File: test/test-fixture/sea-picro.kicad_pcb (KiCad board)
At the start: 2 copper layers, 0 parts

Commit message: tester footprints setup
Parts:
- added C1: 10u, Capacitor_SMD:C_0603_1608Metric, F.Cu at (192.3, 72.7)
- added C10: 100n, Capacitor_SMD:C_0603_1608Metric, F.Cu at (173.1, 56.8)
- added C11: 100n, Capacitor_SMD:C_0603_1608Metric, F.Cu at (190.0, 68.6)
- added C2: 4u7, Capacitor_SMD:C_0603_1608Metric, F.Cu at (170.3, 67.1)
- added C3: 100n, Capacitor_SMD:C_0603_1608Metric, F.Cu at (196.2, 77.9)
- added C4: 100n, Capacitor_SMD:C_0603_1608Metric, F.Cu at (182.5, 60.3)
- added C5: 100n, Capacitor_SMD:C_0603_1608Metric, F.Cu at (198.7, 76.8)
- added C6: 4u7, Capacitor_SMD:C_0603_1608Metric, F.Cu at (207.4, 88.1)
- added C7: 100n, Capacitor_SMD:C_0603_1608Metric, F.Cu at (180.6, 56.1)
- added C8: 100n, Capacitor_SMD:C_0603_1608Metric, F.Cu at (203.1, 84.1)
- added C9: 100n, Capacitor_SMD:C_0603_1608Metric, F.Cu at (168.4, 40.7)
- added D1: WS2812B, LED_SMD:LED_WS2812B_PLCC4_5.0x5.0mm_P3.2mm, F.Cu at (88.3, 121.9)
- added D2: RED, LED_THT:LED_D5.0mm, F.Cu at (127.1, 137.5)
- added D3: GRN, LED_THT:LED_D5.0mm, F.Cu at (125.4, 123.3)
- added F1: 500mA, josh-passives-smt:Fuse_0603_1608Metric, F.Cu at (180.0, 60.1)
- added F2: 500mA, josh-passives-smt:Fuse_0603_1608Metric, F.Cu at (209.9, 88.3)
- added H1: M3, MountingHole:MountingHole_3.2mm_M3_Pad_Via, F.Cu at (146.5, 80.0)
- added H2: M3, MountingHole:MountingHole_3.2mm_M3_Pad_Via, F.Cu at (146.5, 31.0)
- added H3: M3, MountingHole:MountingHole_3.2mm_M3_Pad_Via, F.Cu at (88.5, 80.0)
- added H4: M3, MountingHole:MountingHole_3.2mm_M3_Pad_Via, F.Cu at (88.5, 31.0)
- added H5: M3, MountingHole:MountingHole_3.2mm_M3_Pad_Via, F.Cu at (150.0, 147.3)
- added H6: M3, MountingHole:MountingHole_3.2mm_M3_Pad_Via, F.Cu at (86.7, 142.4)
- added J1: USB_C_Receptacle_USB2.0, josh-connectors:USB_C_Receptacle_HRO_TYPE-C-31-M-12, F.Cu at (167.9, 97.3)
- added J10: RST, Connector_PinHeader_2.54mm:PinHeader_1x03_P2.54mm_Vertical, F.Cu at (182.8, 79.9)
- added J11: SWDCLK, Connector_PinHeader_2.54mm:PinHeader_1x03_P2.54mm_Vertical, F.Cu at (171.3, 71.4)
- added J12: SWD, josh-connectors:SAMTEC_FTSH-105-01-L-DV-R-TR, F.Cu at (195.8, 98.5)
- added J13: SWDIO, Connector_PinHeader_2.54mm:PinHeader_1x03_P2.54mm_Vertical, F.Cu at (195.8, 93.8)
- added J2: Sea-Picro, josh-module:Sea-Picro_EXT_Pogo_Pins, F.Cu at (117.7, 92.8)
- added J3: SP_PWR, Connector_PinHeader_2.54mm:PinHeader_1x02_P2.54mm_Vertical, F.Cu at (164.4, 53.1)
- added J4: Raspberry_Pi_2_3, Connector_PinSocket_2.54mm:PinSocket_2x20_P2.54mm_Vertical, B.Cu at (93.4, 32.3)
- added J5: D- SEL, Connector_PinHeader_2.54mm:PinHeader_1x03_P2.54mm_Vertical, F.Cu at (164.4, 62.4)
- added J6: D+ SEL, Connector_PinHeader_2.54mm:PinHeader_1x03_P2.54mm_Vertical, F.Cu at (164.4, 57.7)
- added J7: USB_PWR, Connector_PinHeader_2.54mm:PinHeader_1x02_P2.54mm_Vertical, F.Cu at (198.8, 89.2)
- added J8: USB_C_Receptacle_USB2.0, josh-connectors:USB_C_Receptacle_HRO_TYPE-C-31-M-12, F.Cu at (201.9, 116.5)
- added J9: SSD1306 OLED, josh-module:OLED_SSD1306_I2C_0.96, F.Cu at (108.4, 116.0)
- added N1: Toggle Clamp, josh-mechanical:GH-201A_X_Adj, F.Cu at (117.6, 62.6)
- added R1: 5K1, Resistor_SMD:R_0603_1608Metric, F.Cu at (196.2, 73.9)
- added R10: 0R0, Resistor_SMD:R_0603_1608Metric, F.Cu at (163.4, 40.6)
- added R11: 0R0, Resistor_SMD:R_0603_1608Metric, F.Cu at (208.1, 80.1)
- added R12: 0R0, Resistor_SMD:R_0603_1608Metric, F.Cu at (178.1, 56.1)
- added R13: 0R0, Resistor_SMD:R_0603_1608Metric, F.Cu at (163.4, 36.6)
- added R14: 0R0, Resistor_SMD:R_0603_1608Metric, F.Cu at (168.4, 44.7)
- added R15: 0R0, Resistor_SMD:R_0603_1608Metric, F.Cu at (203.1, 80.1)
- added R16: 0R0, Resistor_SMD:R_0603_1608Metric, F.Cu at (192.5, 64.7)
- added R17: 0R0, Resistor_SMD:R_0603_1608Metric, F.Cu at (185.0, 60.3)
- added R18: 0R0, Resistor_SMD:R_0603_1608Metric, F.Cu at (182.3, 64.3)
- added R19: 0R0, Resistor_SMD:R_0603_1608Metric, F.Cu at (200.6, 84.9)
- added R2: 10K, Resistor_SMD:R_0603_1608Metric, F.Cu at (208.1, 84.1)
- added R20: 0R0, Resistor_SMD:R_0603_1608Metric, F.Cu at (210.7, 84.3)
- added R21: 0R0, Resistor_SMD:R_0603_1608Metric, F.Cu at (177.5, 60.1)
- added R22: 0R0, Resistor_SMD:R_0603_1608Metric, F.Cu at (180.6, 52.1)
- added R23: 0R0, Resistor_SMD:R_0603_1608Metric, F.Cu at (195.0, 69.8)
- added R24: 0R0, Resistor_SMD:R_0603_1608Metric, F.Cu at (200.6, 80.9)
- added R25: 0R0, Resistor_SMD:R_0603_1608Metric, F.Cu at (170.9, 44.8)
- added R26: 0R0, Resistor_SMD:R_0603_1608Metric, F.Cu at (192.5, 68.7)
- added R27: 0R0, Resistor_SMD:R_0603_1608Metric, F.Cu at (163.4, 44.6)
- added R28: 0R0, Resistor_SMD:R_0603_1608Metric, F.Cu at (183.1, 56.2)
- added R29: 0R0, Resistor_SMD:R_0603_1608Metric, F.Cu at (165.9, 40.6)
- added R3: 5K1, Resistor_SMD:R_0603_1608Metric, F.Cu at (187.5, 68.6)
- added R30: 0R0, Resistor_SMD:R_0603_1608Metric, F.Cu at (204.9, 88.1)
- added R31: 0R0, Resistor_SMD:R_0603_1608Metric, F.Cu at (203.7, 76.1)
- added R32: 0R0, Resistor_SMD:R_0603_1608Metric, F.Cu at (178.1, 52.1)
- added R33: 10K, Resistor_SMD:R_0603_1608Metric, F.Cu at (173.1, 52.8)
- added R34: 10K, Resistor_SMD:R_0603_1608Metric, F.Cu at (187.3, 64.3)
- added R35: 1K, Resistor_SMD:R_0603_1608Metric, F.Cu at (168.1, 48.7)
- added R36: 1K, Resistor_SMD:R_0603_1608Metric, F.Cu at (205.6, 80.1)
- added R37: 10K, Resistor_SMD:R_0603_1608Metric, F.Cu at (165.9, 44.6)
- added R38: 10K, Resistor_SMD:R_0603_1608Metric, F.Cu at (175.6, 56.1)
- added R39: 0R0, Resistor_SMD:R_0603_1608Metric, F.Cu at (175.9, 48.1)
- added R4: 0R0, Resistor_SMD:R_0603_1608Metric, F.Cu at (175.6, 52.1)
- added R40: 10K, Resistor_SMD:R_0603_1608Metric, F.Cu at (170.6, 48.8)
- added R41: 10K, Resistor_SMD:R_0603_1608Metric, F.Cu at (201.2, 76.1)
- added R42: 0R, Resistor_SMD:R_0603_1608Metric, F.Cu at (189.8, 64.6)
- added R43: 100K, Resistor_SMD:R_0603_1608Metric, F.Cu at (198.7, 72.8)
- added R44: 100K, Resistor_SMD:R_0603_1608Metric, F.Cu at (209.7, 92.3)
- added R5: 0R0, Resistor_SMD:R_0603_1608Metric, F.Cu at (173.4, 48.1)
- added R6: 4K7, Resistor_SMD:R_0603_1608Metric, F.Cu at (205.6, 84.1)
- added R7: 4K7, Resistor_SMD:R_0603_1608Metric, F.Cu at (184.8, 64.3)
- added R8: 100K, Resistor_SMD:R_0603_1608Metric, F.Cu at (187.6, 60.3)
- added R9: 0R0, Resistor_SMD:R_0603_1608Metric, F.Cu at (170.6, 53.4)
- added RN1: 1K, Resistor_SMD:R_Array_Convex_4x0603, F.Cu at (197.0, 81.9)
- added RN2: 1K, Resistor_SMD:R_Array_Convex_4x0603, F.Cu at (192.5, 76.8)
- added RN3: 1K, Resistor_SMD:R_Array_Convex_4x0603, F.Cu at (206.0, 92.2)
- added RN4: 1K, Resistor_SMD:R_Array_Convex_4x0603, F.Cu at (178.6, 64.2)
- added RN5: 1K, Resistor_SMD:R_Array_Convex_4x0603, F.Cu at (188.6, 72.6)
- added RN6: 1K, Resistor_SMD:R_Array_Convex_4x0603, F.Cu at (164.5, 48.7)
- added SW1: PASS, josh-buttons-switches:SW_Push_PTS645, F.Cu at (136.6, 123.5)
- added SW2: FAIL, josh-buttons-switches:SW_Push_PTS645, F.Cu at (137.3, 137.9)
- added SW3: SW_SPDT, josh-buttons-switches:SW_SPDT_PCM12, F.Cu at (165.1, 69.6)
- added SW4: SW_SPDT, josh-buttons-switches:SW_SPDT_PCM12, F.Cu at (199.1, 105.7)
- added SW5: SW_SPDT, josh-buttons-switches:SW_SPDT_PCM12, F.Cu at (176.5, 78.7)
- added SW6: SW_SPDT, josh-buttons-switches:SW_SPDT_PCM12, F.Cu at (185.0, 87.1)
- added TP1: SP_SWDIO, josh-test-point:TestPoint_Pogo_1.4mm_Drill_Off_Center, F.Cu at (126.9, 88.4)
- added TP2: SP_SWDCLK, josh-test-point:TestPoint_Pogo_1.4mm_Drill_Off_Center, F.Cu at (126.4, 97.1)
- added TP3: SP_RUN, josh-test-point:TestPoint_Pogo_1.4mm_Drill_Off_Center, F.Cu at (129.1, 91.2)
- added TP4: SP_BOOT, josh-test-point:TestPoint_Pogo_1.4mm_Drill_Off_Center, F.Cu at (128.7, 88.4)
- added U1: AP22653, Package_TO_SOT_SMD:SOT-23-6, F.Cu at (192.4, 81.4)
- added U2: USBLC6-2SC6, Package_TO_SOT_SMD:SOT-23-6, F.Cu at (208.8, 114.6)
- added U3: USBLC6-2SC6, Package_TO_SOT_SMD:SOT-23-6, F.Cu at (174.0, 61.4)
- added U4: 74HC595, Package_SO:SOIC-16_3.9x9.9mm_P1.27mm, F.Cu at (167.8, 78.8)
- added U5: 74HC595, Package_SO:SOIC-16_3.9x9.9mm_P1.27mm, F.Cu at (179.3, 98.9)
- added U6: 74HC595, Package_SO:SOIC-16_3.9x9.9mm_P1.27mm, F.Cu at (167.8, 87.2)
- added U7: ADC101C027CIMK, Package_TO_SOT_SMD:SOT-23-6, F.Cu at (208.8, 119.8)
- added U8: ADC101C027CIMK, Package_TO_SOT_SMD:SOT-23-6, F.Cu at (174.0, 66.5)

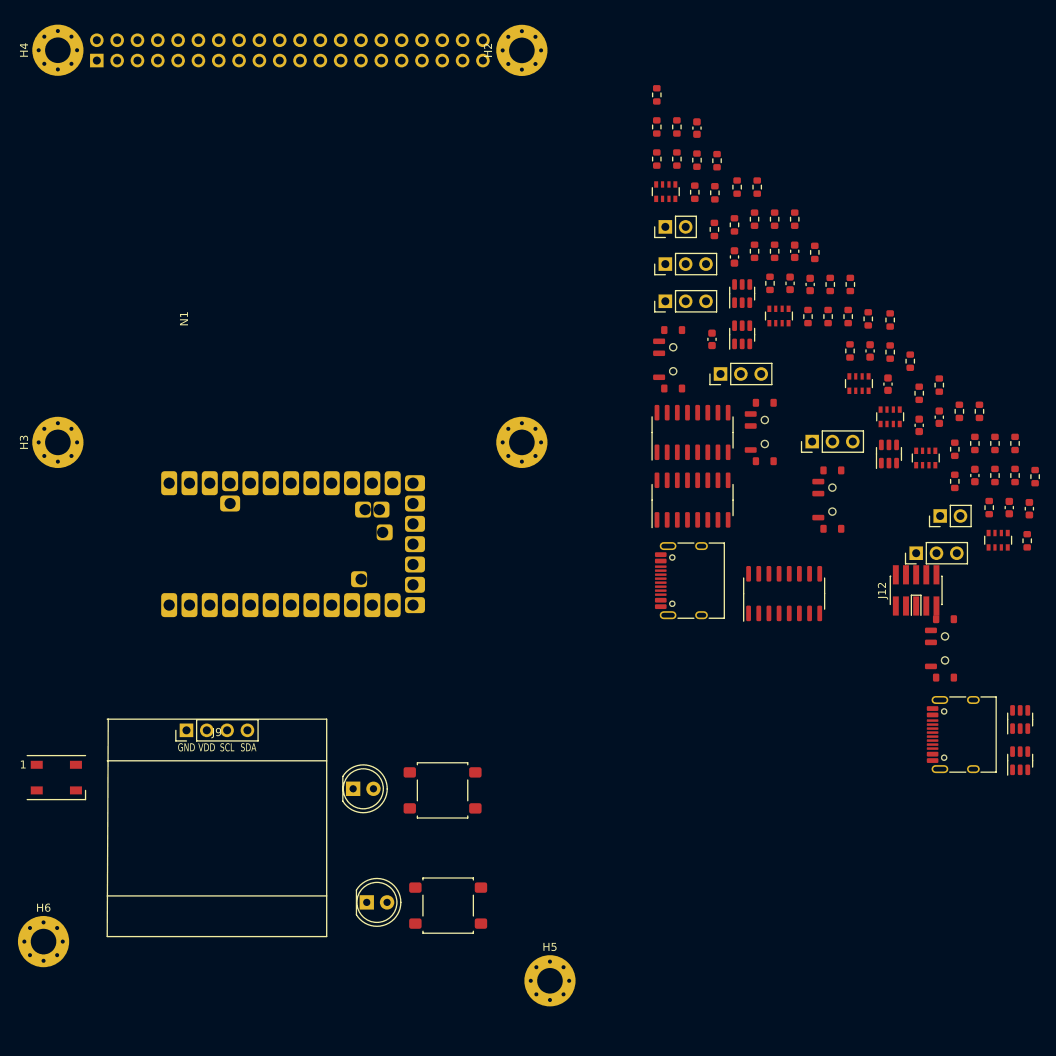
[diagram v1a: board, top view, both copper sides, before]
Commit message: rough mechanical layout
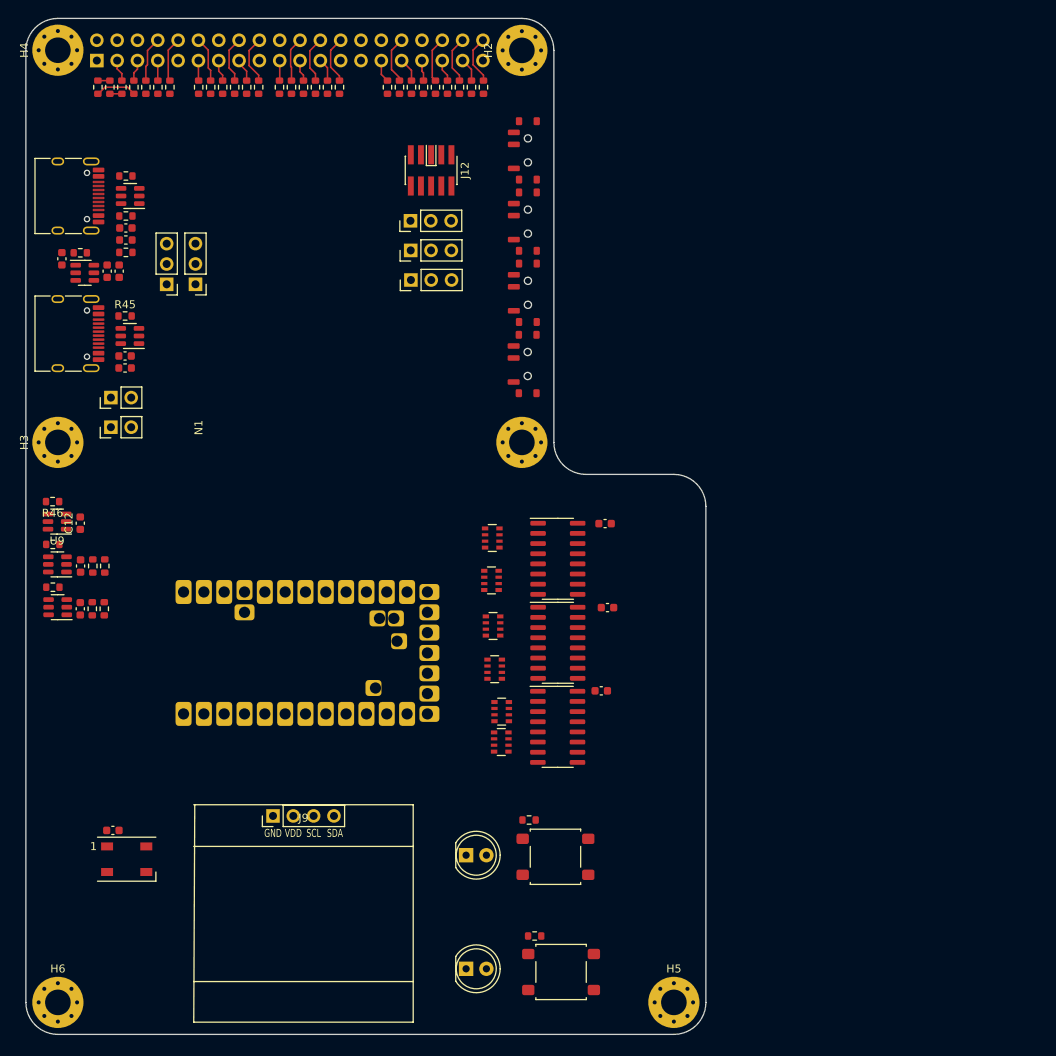
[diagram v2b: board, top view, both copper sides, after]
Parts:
- removed R35, R36: 1K, Resistor_SMD:R_0603_1608Metric
- removed R40, R41: 10K, Resistor_SMD:R_0603_1608Metric
- added C12: 100n, Capacitor_SMD:C_0603_1608Metric, F.Cu at (91.3, 90.1)
- added R45: 5K1, Resistor_SMD:R_0603_1608Metric, F.Cu at (96.9, 64.2)
- added R46: 0R0, Resistor_SMD:R_0603_1608Metric, F.Cu at (87.8, 87.4)
- added U9: ADC101C027CIMK, Package_TO_SOT_SMD:SOT-23-6, F.Cu at (88.4, 89.9)
- R18, R20, R22, R24, R26, R28: value 0R0 -> 10K
- R31, R32: value 0R0 -> 1K
- moved U2 129.1 mm to (97.5, 49.2), turned to 180 degrees
- moved J8 123.0 mm to (89.5, 66.4), turned to -90 degrees
- moved U7 121.8 mm to (88.5, 100.6), turned to 180 degrees
- moved R6 120.8 mm to (95.0, 35.6), turned to -90 degrees
- moved R44 116.8 mm to (92.9, 95.5), turned to -90 degrees
- moved R2 114.6 mm to (97.0, 56.2), turned to 0 degrees
- moved F2 114.4 mm to (96.9, 70.7), turned to 180 degrees
- moved C3 112.8 mm to (95.4, 128.5), turned to 0 degrees
- moved C6 112.1 mm to (96.9, 69.2), turned to 0 degrees
- moved C5 111.4 mm to (89.0, 57.0)
- moved R11 111.3 mm to (106.1, 35.6)
- moved R43 109.5 mm to (92.8, 100.8), turned to -90 degrees
- moved R30 109.3 mm to (109.1, 35.6)
- moved R42 105.8 mm to (87.9, 92.8), turned to 0 degrees
- moved J7 104.7 mm to (95.1, 74.4)
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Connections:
- D2 pad 1: Net-(D2-Pad1) -> /LED_FAIL
- D3 pad 1: Net-(D3-Pad1) -> /LED_PASS
- J8 pad A5: unconnected-(J8-PadA5) -> /CC_SENSE
- J8 pad B5: unconnected-(J8-PadB5) -> /CC_SENSE
- R37 pad 1: +3V3 -> /SP_VBUS
- R37 pad 2: /SHORT_DETECT_5V0 -> /SHT_CTRL_5V
- R38 pad 1: +3V3 -> +3.3VP
- R38 pad 2: /SHORT_DETECT_3V3 -> /SHT_CTRL_3V3
- R43 pad 1: /SHORT_DETECT_5V0 -> /SHT_CTRL_5V
- R44 pad 1: /SHORT_DETECT_3V3 -> /SHT_CTRL_3V3
- U3 pad 1: /USB_HOST- -> /USB_HOST+
- U3 pad 3: /USB_HOST+ -> /USB_HOST-
- U3 pad 4: Net-(J8-PadA6) -> Net-(J8-PadA7)
- U3 pad 6: Net-(J8-PadA7) -> Net-(J8-PadA6)
- U7 pad 3: /SHORT_DETECT_5V0 -> /SHT_CTRL_5V
- U8 pad 3: /SHORT_DETECT_3V3 -> /SHT_CTRL_3V3
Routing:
- net Net-(J4-Pad40): track 0.00 -> 6.09 mm
- net Net-(J4-Pad18): track 0.00 -> 6.08 mm
- net Net-(J4-Pad26): track 0.00 -> 6.02 mm
- net Net-(J4-Pad32): track 0.00 -> 5.99 mm
- net Net-(J4-Pad38): track 0.00 -> 5.95 mm
- net Net-(J4-Pad24): track 0.00 -> 5.88 mm
- net Net-(J4-Pad16): track 0.00 -> 5.85 mm
- net Net-(J4-Pad36): track 0.00 -> 5.73 mm
- net Net-(J4-Pad12): track 0.00 -> 5.68 mm
- net Net-(J4-Pad8): track 0.00 -> 5.66 mm
- net Net-(J4-Pad10): track 0.00 -> 5.64 mm
- net Net-(J4-Pad22): track 0.00 -> 5.57 mm
- net /I2C_SCL: track 0.00 -> 5.20 mm
- net Net-(J4-Pad31): track 0.00 -> 3.01 mm
- net Net-(J4-Pad37): track 0.00 -> 2.96 mm
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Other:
- board outline added: 85 x 127 mm

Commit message: test/quick-test-fixture
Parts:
- added H7: M2, MountingHole:MountingHole_2.2mm_M2_DIN965_Pad, F.Cu at (119.5, 106.4)
- added kibuzzard-62E5E34B: G***, kibuzzard-62E5E34B, F.Cu at (142.8, 45.3)
- added kibuzzard-62E5E354: G***, kibuzzard-62E5E354, F.Cu at (142.8, 41.6)
- added kibuzzard-62E5E361: G***, kibuzzard-62E5E361, F.Cu at (142.8, 50.5)
- added kibuzzard-62E5E361: G***, kibuzzard-62E5E361, F.Cu at (142.8, 68.3)
- added kibuzzard-62E5E361: G***, kibuzzard-62E5E361, F.Cu at (142.8, 59.4)
- added kibuzzard-62E5E382: G***, kibuzzard-62E5E382, F.Cu at (143.2, 54.2)
- added kibuzzard-62E5E382: G***, kibuzzard-62E5E382, F.Cu at (143.2, 63.2)
- added kibuzzard-62E5E382: G***, kibuzzard-62E5E382, F.Cu at (143.2, 72.1)
- added kibuzzard-62E5E3DC: G***, kibuzzard-62E5E3DC, F.Cu at (139.7, 43.2)
- added kibuzzard-62E5E412: G***, kibuzzard-62E5E412, F.Cu at (139.7, 61.3)
- added kibuzzard-62E5E428: G***, kibuzzard-62E5E428, F.Cu at (139.7, 51.9)
- added kibuzzard-62E5E442: G***, kibuzzard-62E5E442, F.Cu at (139.7, 69.8)
- added kibuzzard-62E5E5A0: G***, kibuzzard-62E5E5A0, F.Cu at (109.7, 55.0)
- added kibuzzard-62E5E5AB: G***, kibuzzard-62E5E5AB, F.Cu at (110.1, 60.4)
- added kibuzzard-62E5E5C3: G***, kibuzzard-62E5E5C3, F.Cu at (103.8, 51.8)
- added kibuzzard-62E5E5E6: G***, kibuzzard-62E5E5E6, F.Cu at (104.2, 74.4)
- added kibuzzard-62E5E5F2: G***, kibuzzard-62E5E5F2, F.Cu at (103.6, 78.1)
- added kibuzzard-62E5EE8F: G***, kibuzzard-62E5EE8F, F.Cu at (141.2, 136.6)
- added kibuzzard-62E5EE98: G***, kibuzzard-62E5EE98, F.Cu at (141.1, 151.2)
- added kibuzzard-62E5EEC8: G***, kibuzzard-62E5EEC8, F.Cu at (154.6, 136.6)
- added kibuzzard-62E5EECF: G***, kibuzzard-62E5EECF, F.Cu at (154.7, 151.2)
- added kibuzzard-62E60834: G***, kibuzzard-62E60834, F.Cu at (97.1, 132.1)
- added kibuzzard-62E61122: G***, kibuzzard-62E61122, F.Cu at (119.5, 44.3)
- added kibuzzard-62E61157: G***, kibuzzard-62E61157, F.Cu at (115.6, 41.3)
- added kibuzzard-62E615DC: G***, kibuzzard-62E615DC, F.Cu at (115.7, 46.6)
- added kibuzzard-62E61612: G***, kibuzzard-62E61612, F.Cu at (92.8, 40.6)
- moved R34 104.7 mm to (129.7, 38.6), turned to 90 degrees
- moved R33 101.4 mm to (104.0, 35.6), turned to -90 degrees
- moved J12 36.3 mm to (99.2, 40.9), turned to 0 degrees
- moved J10 27.7 mm to (105.5, 46.4), turned to 180 degrees
- moved J13 25.8 mm to (108.6, 46.4), turned to 180 degrees
- moved J11 24.9 mm to (111.6, 46.4), turned to 180 degrees
- moved SW6 8.90 mm to (146.9, 70.2)
- moved SW4 8.90 mm to (146.9, 61.3)
- moved RN2 6.15 mm to (145.0, 102.5)
- moved C3 4.20 mm to (95.4, 124.3)
- moved D1 4.20 mm to (97.1, 127.9)
- moved SW1 4.00 mm to (154.7, 131.6)
- moved RN5 3.87 mm to (145.0, 106.2)
- moved SW2 3.30 mm to (154.7, 146.2)
- moved RN6 2.72 mm to (145.0, 95.8)
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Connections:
- net /SHT_CTRL_3V3 renamed /SHORT_DETECT_3V3
- net /SHT_CTRL_5V renamed /SHORT_DETECT_5V0
- J12 pad 1: +3.3VP -> +3V3
- RN1 pad 5: /IO0 -> /IO7
- RN1 pad 6: /IO1 -> /IO6
- RN1 pad 7: /IO2 -> /IO5
- RN1 pad 8: /IO3 -> /IO4
- RN2 pad 5: /IO8 -> /IO21
- RN2 pad 6: /IO9 -> /IO16
- RN2 pad 7: /IO12 -> /IO15
- RN2 pad 8: /IO13 -> /IO14
- RN3 pad 5: /IO23 -> /IO29
- RN3 pad 6: /IO20 -> /IO28
- RN3 pad 7: /IO22 -> /IO27
- RN4 pad 5: /IO4 -> /IO3
- RN4 pad 6: /IO5 -> /IO2
- RN4 pad 7: /IO6 -> /IO1
- RN4 pad 8: /IO7 -> /IO0
- RN5 pad 5: /IO14 -> /IO13
- RN5 pad 6: /IO15 -> /IO12
- RN5 pad 7: /IO16 -> /IO9
- RN5 pad 8: /IO21 -> /IO8
- RN6 pad 5: /IO27 -> /IO22
- RN6 pad 6: /IO28 -> /IO20
- RN6 pad 7: /IO29 -> /IO23
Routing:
- net +3V3: track 1.50 -> 244.4 mm, vias 0 -> 8
- net /SW_PASS: track 0.00 -> 162.7 mm, vias 0 -> 6
- net +5V: track 0.00 -> 157.9 mm, vias 0 -> 7
- net /SP_RUN: track 0.00 -> 147.2 mm, vias 0 -> 6
- net /SW_FAIL: track 0.00 -> 146.1 mm, vias 0 -> 2
- net /LED_FAIL: track 0.00 -> 142.2 mm, vias 0 -> 2
- net /I2C_SCL: track 5.20 -> 135.3 mm
- net /SR_CLK: track 0.00 -> 128.9 mm, vias 0 -> 6
- net /I2C_SDA: track 1.50 -> 129.9 mm, vias 0 -> 4
- net /LED_PASS: track 0.00 -> 128.4 mm, vias 0 -> 2
- net /SR_nCLR: track 0.00 -> 126.2 mm, vias 0 -> 6
- net /SP_BOOT: track 0.00 -> 109.0 mm, vias 0 -> 6
- net /SHORT_DETECT_5V0: track 0.00 -> 105.6 mm, vias 0 -> 8
- net /SHORT_DETECT_3V3: track 0.00 -> 104.7 mm, vias 0 -> 6
- net /SR_RCLK: track 0.00 -> 98.2 mm, vias 0 -> 4
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- added copper zone on B.Cu, net GND

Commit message: update cpy test code
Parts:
- removed kibuzzard-62E61612: G***, kibuzzard-62E61612
- added kibuzzard-62E650F2: G***, kibuzzard-62E650F2, F.Cu at (94.7, 40.9)
- added kibuzzard-62E65108: G***, kibuzzard-62E65108, F.Cu at (89.1, 42.8)
- added kibuzzard-62E65113: G***, kibuzzard-62E65113, F.Cu at (88.8, 72.8)
- added kibuzzard-62E651F0: G***, kibuzzard-62E651F0, F.Cu at (163.3, 107.2)
- added kibuzzard-62E65209: G***, kibuzzard-62E65209, F.Cu at (166.8, 115.9)
- added kibuzzard-62E6521B: G***, kibuzzard-62E6521B, F.Cu at (166.8, 96.5)
- moved kibuzzard-62E5E412 0.40 mm to (139.7, 61.7)
